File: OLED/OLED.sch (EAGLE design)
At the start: 15 parts

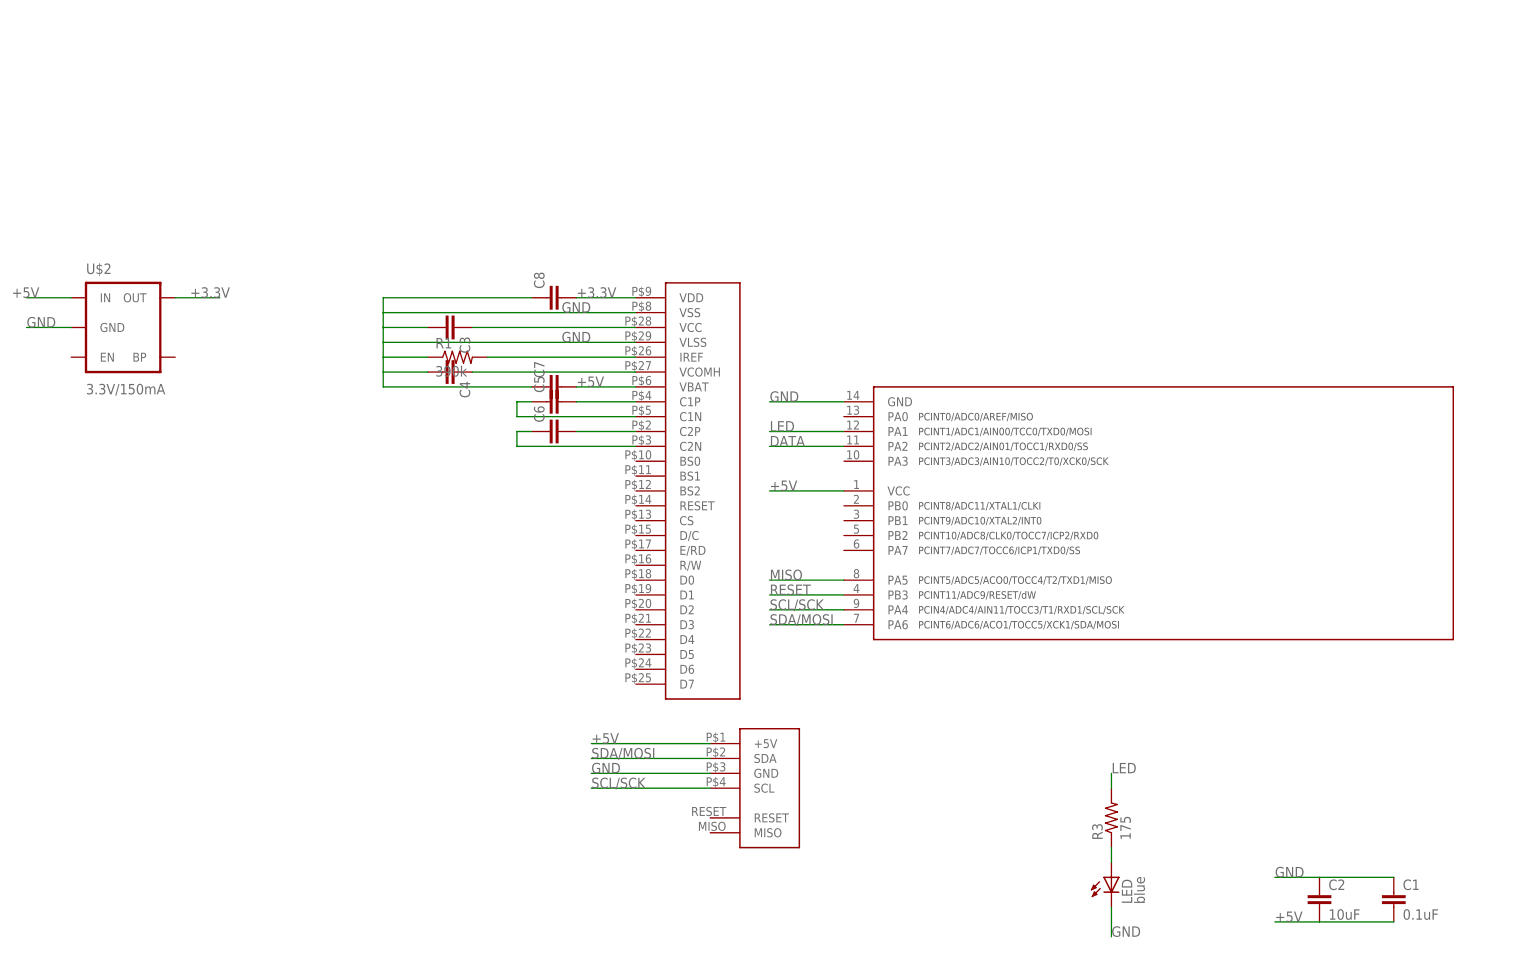
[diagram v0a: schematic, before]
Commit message: Checking in current version of OLED board
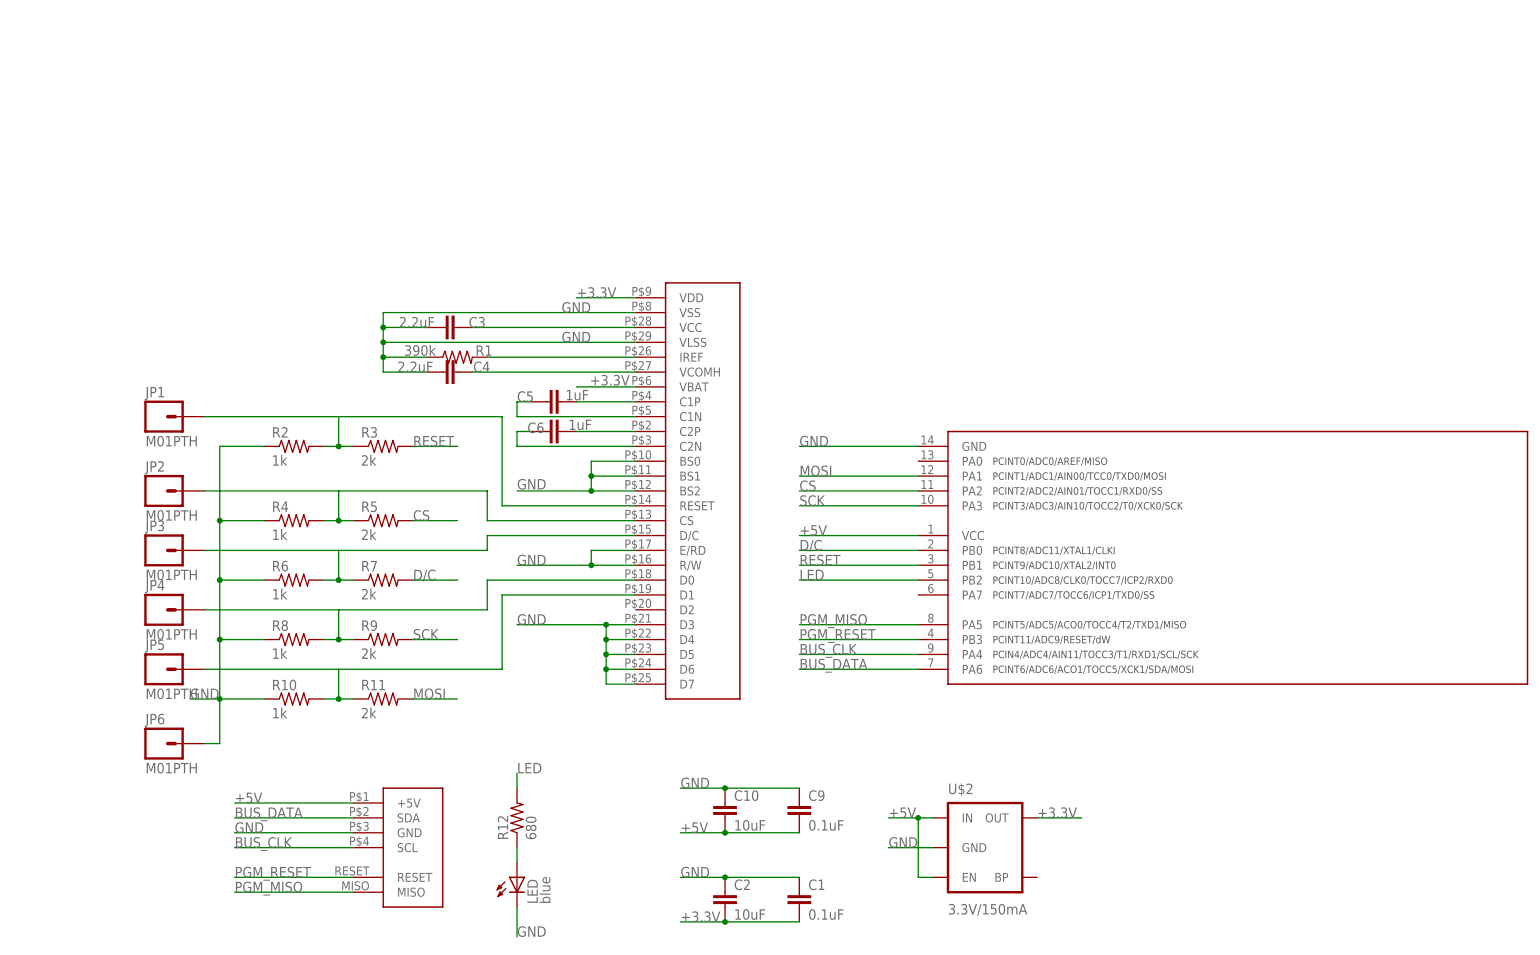
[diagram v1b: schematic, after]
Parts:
- removed C7, C8: (no value), SparkFun-Capacitors:CAP0805
- added C10: 10uF, SparkFun-Capacitors:CAP0805
- added C9: 0.1uF, SparkFun-Capacitors:CAP0805
- added JP1, JP2, JP3, JP4, JP5, JP6: M01PTH, SparkFun-Connectors:M01PTH
- added R10, R2, R4, R6, R8: 1k, SparkFun-Resistors:RESISTOR0805-RES
- added R11, R5, R7, R9: 2k, SparkFun-Resistors:RESISTOR0805-RES
- added R12: 680, SparkFun-Passives:RESISTOR0805-RES
- C3, C4: value (none) -> 2.2uF
- C5, C6: value (none) -> 1uF
- R3: value 175 -> 2k; device SparkFun-Passives:RESISTOR0805-RES -> SparkFun-Resistors:RESISTOR0805-RES
- U$4: value FOOTPRINTDOUBLE -> FOOTPRINTDOUBLE-NODIM; device IntegerLabs:FOOTPRINTDOUBLE -> IntegerLabs:FOOTPRINTDOUBLE-NODIM
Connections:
- net SCL/SCK renamed BUS_CLK
- net SDA/MOSI renamed BUS_DATA
- removed net DATA: U$3.PA2
- removed net MISO: U$3.PA5
- new net CS: R5.2, U$3.PA2
- new net D/C: R7.2, U$3.PB0
- new net MOSI: R11.2, U$3.PA1
- new net N$13: JP3.1, R6.2, R7.1, U$1.D/C
- new net N$14: JP2.1, R4.2, R5.1, U$1.CS
- new net N$15: JP1.1, R2.2, R3.1, U$1.RESET
- new net N$7: JP5.1, R10.2, R11.1, U$1.D1
- new net N$8: JP4.1, R8.2, R9.1, U$1.D0
- new net PGM_MISO: U$3.PA5, U$4.MISO
- new net PGM_RESET: U$3.PB3, U$4.RESET
- new net SCK: R9.2, U$3.PA3
- net +3.3V: now also C1.2, C2.2, U$1.VBAT; no longer C8.2
- net +5V: now also C10.2, C9.2, U$2.EN; no longer C1.2, C2.2, C7.2, U$1.VBAT
- net GND: now also C10.1, C9.1, JP6.1, R10.1, R2.1, R4.1, R6.1, R8.1, U$1.BS0, U$1.BS1, U$1.BS2, U$1.D3, U$1.D4, U$1.D5, U$1.D6, U$1.D7, U$1.E/RD, U$1.R/W; no longer C7.1, C8.1
- net LED: now also R12.2, U$3.PB2; no longer R3.2, U$3.PA1
- net N$5: now also R12.1; no longer R3.1
- net RESET: now also R3.2, U$3.PB1; no longer U$3.PB3
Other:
- moved on the sheet: C1, C2, LED, R3, U$2

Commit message: New OLED design for v2 footprint.
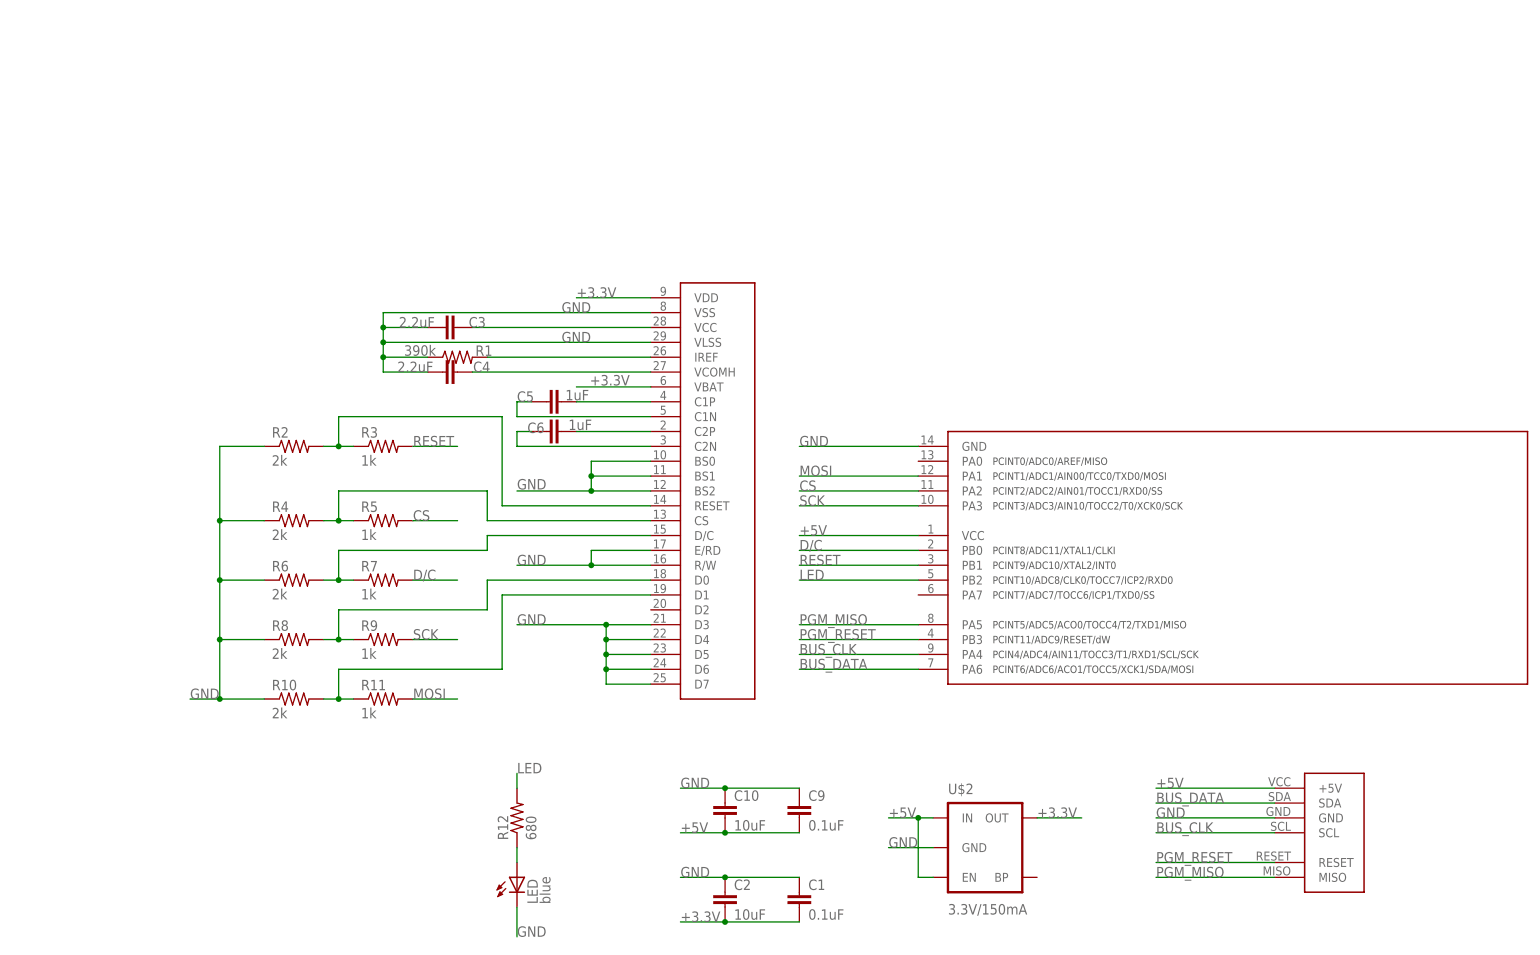
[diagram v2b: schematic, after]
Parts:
- removed JP1, JP2, JP3, JP4, JP5, JP6: M01PTH, SparkFun-Connectors:M01PTH
- removed U$4: FOOTPRINTDOUBLE-NODIM, IntegerLabs:FOOTPRINTDOUBLE-NODIM
- added U$5: FOOTPRINTFOOTPRINT-2, IntegerLabs:FOOTPRINTFOOTPRINT-2
- R10, R2, R4, R6, R8: value 1k -> 2k
- R11, R3, R5, R7, R9: value 2k -> 1k
- U$1: value OLED -> OLEDREVERSE; device IntegerLabs:OLED -> IntegerLabs:OLEDREVERSE
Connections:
- net +5V: now also U$5.+5V; no longer U$4.+5V
- net BUS_CLK: now also U$5.SCL; no longer U$4.SCL
- net BUS_DATA: now also U$5.SDA; no longer U$4.SDA
- net GND: now also U$5.GND; no longer JP6.1, U$4.GND
- net N$13: no longer JP3.1
- net N$14: no longer JP2.1
- net N$15: no longer JP1.1
- net N$7: no longer JP5.1
- net N$8: no longer JP4.1
- net PGM_MISO: now also U$5.MISO; no longer U$4.MISO
- net PGM_RESET: now also U$5.RESET; no longer U$4.RESET

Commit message: Changed OLED board to use ATmega328P instead of ATtiny841.
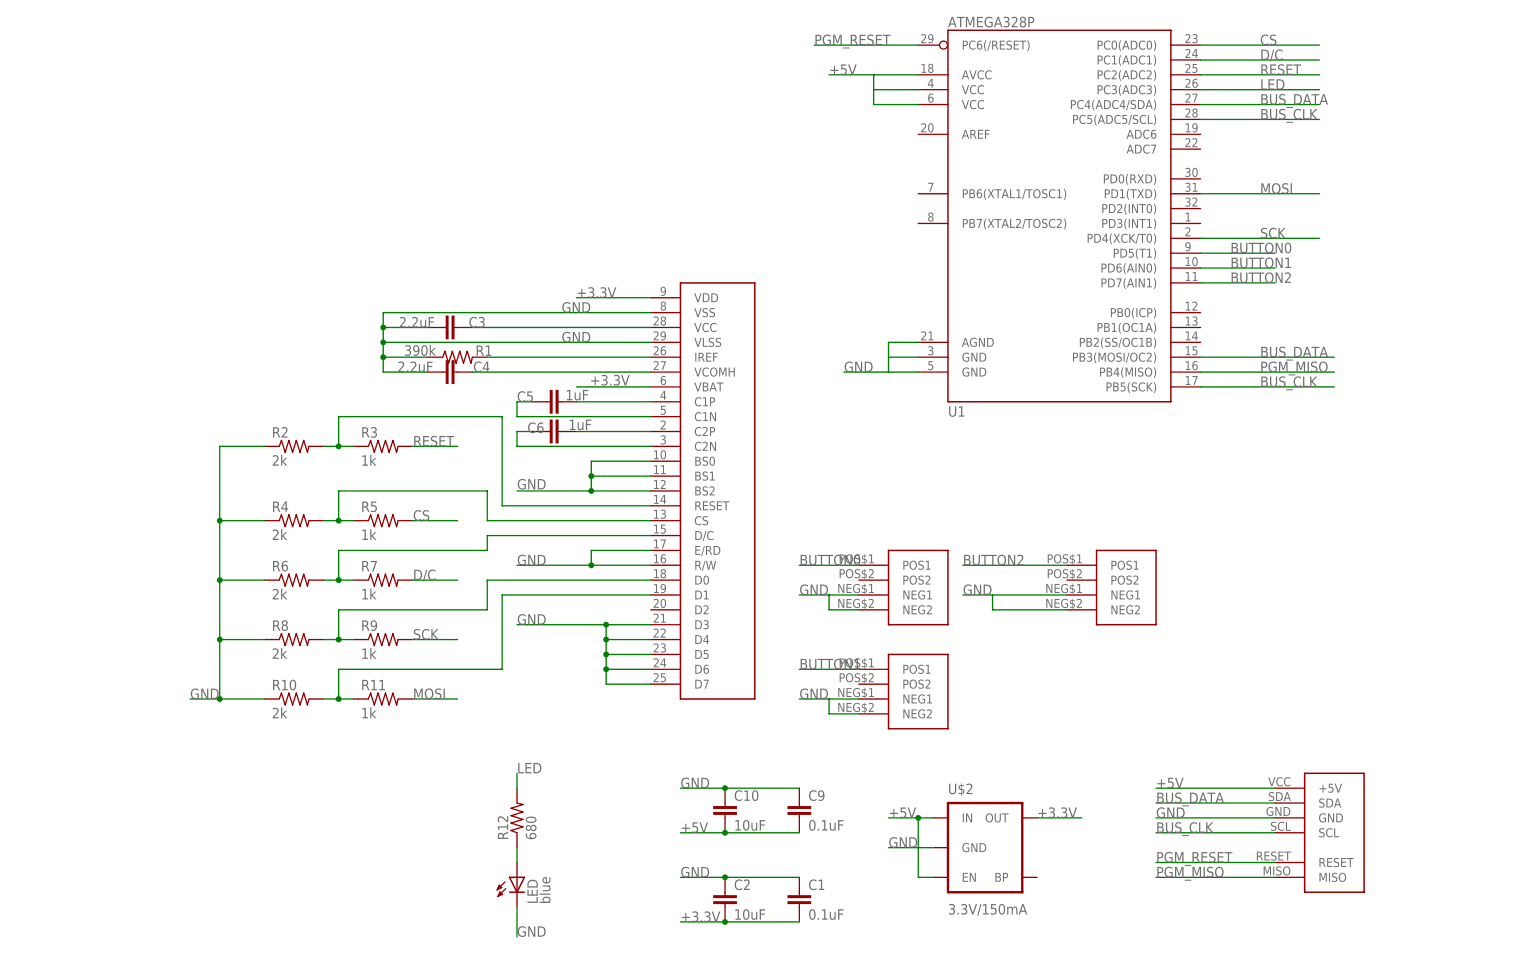
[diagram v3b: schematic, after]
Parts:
- added U$4, U$6: TACT-SWITCHBOURNS-7914J, IntegerLabs:TACT-SWITCHBOURNS-7914J
- added U1: ATMEGA328P, SparkFun-DigitalIC:ATMEGA328_SMT
- U$3: value TINY841 -> TACT-SWITCHBOURNS-7914J; device IntegerLabs:TINY841 -> IntegerLabs:TACT-SWITCHBOURNS-7914J
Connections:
- new net BUTTON0: U$3.POS1, U1.PD5(T1)
- new net BUTTON1: U$6.POS1, U1.PD6(AIN0)
- new net BUTTON2: U$4.POS1, U1.PD7(AIN1)
- net +5V: now also U1.AVCC, U1.VCC@1, U1.VCC@2; no longer U$3.VCC
- net BUS_CLK: now also U1.PB5(SCK), U1.PC5(ADC5/SCL); no longer U$3.PA4
- net BUS_DATA: now also U1.PB3(MOSI/OC2), U1.PC4(ADC4/SDA); no longer U$3.PA6
- net CS: now also U1.PC0(ADC0); no longer U$3.PA2
- net D/C: now also U1.PC1(ADC1); no longer U$3.PB0
- net GND: now also U$3.NEG1, U$3.NEG2, U$4.NEG1, U$4.NEG2, U$6.NEG1, U$6.NEG2, U1.AGND, U1.GND@1, U1.GND@2; no longer U$3.GND
- net LED: now also U1.PC3(ADC3); no longer U$3.PB2
- net MOSI: now also U1.PD1(TXD); no longer U$3.PA1
- net PGM_MISO: now also U1.PB4(MISO); no longer U$3.PA5
- net PGM_RESET: now also U1.PC6(/RESET); no longer U$3.PB3
- net RESET: now also U1.PC2(ADC2); no longer U$3.PB1
- net SCK: now also U1.PD4(XCK/T0); no longer U$3.PA3
